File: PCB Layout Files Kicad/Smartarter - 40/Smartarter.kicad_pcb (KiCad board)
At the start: 2 copper layers, 135.5 x 154.5 mm, 44 parts, among them J1 Screw_Terminal_01x03, J2 Screw_Terminal_01x03, K1 onRelay, K2 offRelay, Q1 BC547, Q2 BC547, Q3 BC547, SW1 SW_Push, U1 74164, U2 KCSA02-107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

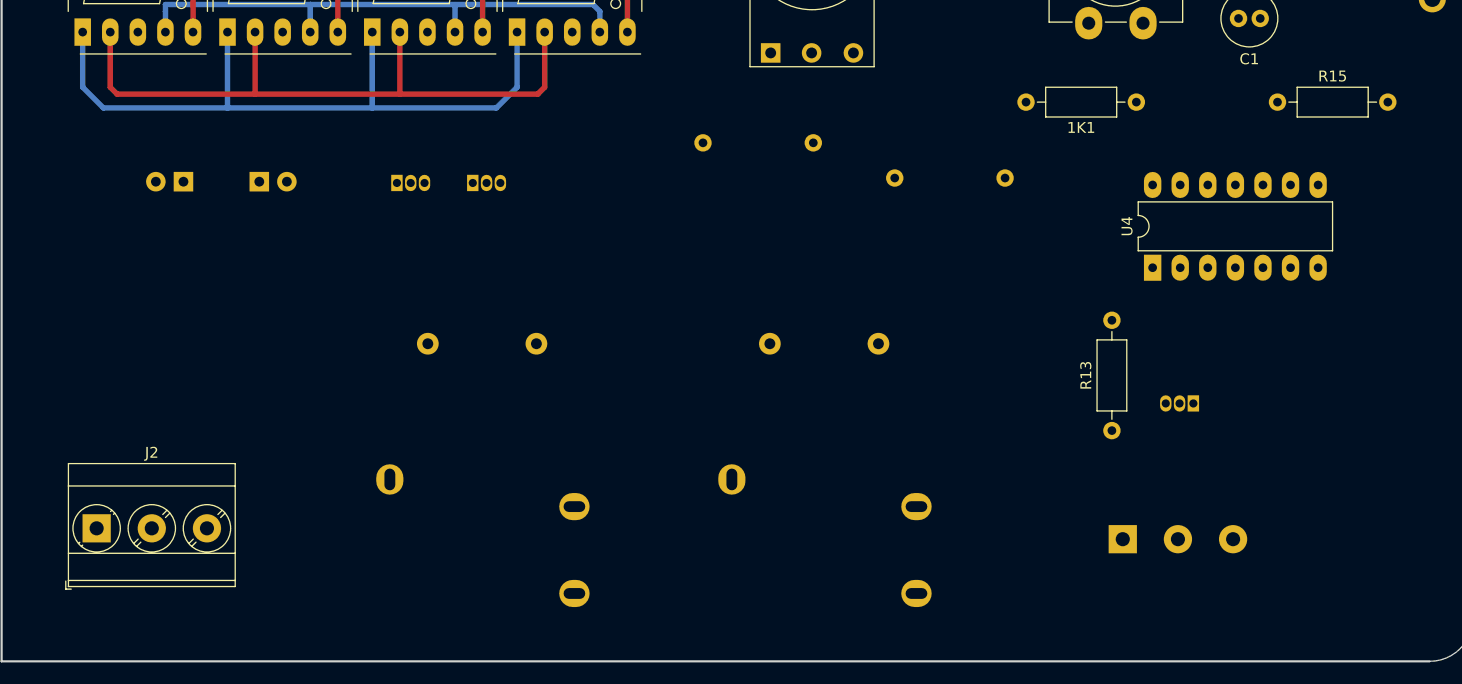
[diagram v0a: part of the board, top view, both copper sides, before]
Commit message: inductor and full wave rectifier implemented in both schematic and layout
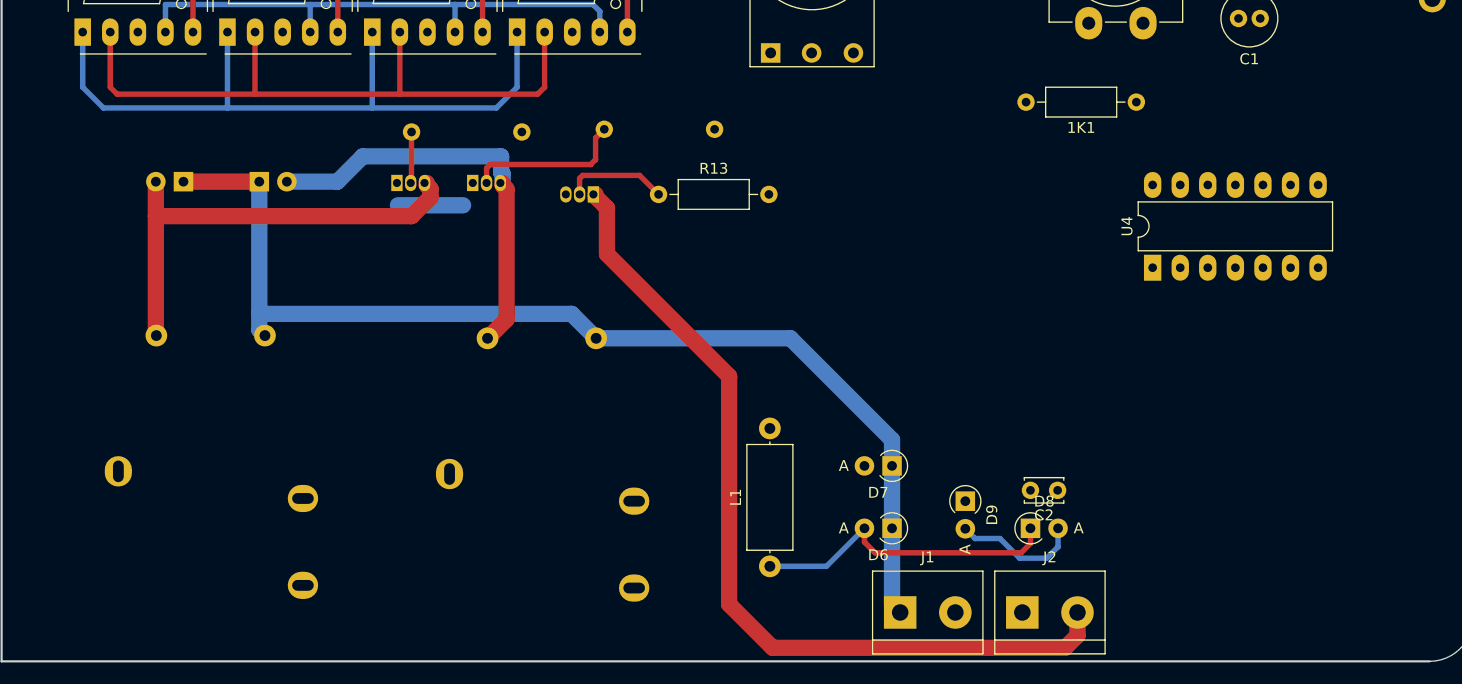
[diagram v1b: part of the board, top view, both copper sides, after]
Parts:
- removed R15: R, Resistor_THT:R_Axial_DIN0207_L6.3mm_D2.5mm_P10.16mm_Horizontal
- added C2: C_Small, Capacitor_THT:C_Disc_D3.4mm_W2.1mm_P2.50mm, F.Cu at (146.2, 164.8)
- added D6: DIODE, Diode_THT:D_A-405_P2.54mm_Vertical_AnodeUp, F.Cu at (131.0, 168.2)
- added D7: DIODE, Diode_THT:D_A-405_P2.54mm_Vertical_AnodeUp, F.Cu at (131.0, 162.5)
- added D8: DIODE, Diode_THT:D_A-405_P2.54mm_Vertical_AnodeUp, F.Cu at (143.8, 168.2)
- added D9: DIODE, Diode_THT:D_A-405_P2.54mm_Vertical_AnodeUp, F.Cu at (137.8, 165.8)
- added L1: INDUCTOR, Inductor_THT:L_Axial_L9.5mm_D4.0mm_P12.70mm_Horizontal_Fastron_SMCC, F.Cu at (119.8, 171.8)
- J1: value Screw_Terminal_01x03 -> Screw_Terminal_01x02; footprint Connector_Phoenix:TerminalBlock_Phoenix_MKDS-3-3-5.08_1x03_P5.08mm_Horizontal -> TerminalBlock:TerminalBlock_bornier-2_P5.08mm; moved to F.Cu
- J2: value Screw_Terminal_01x03 -> Screw_Terminal_01x02; footprint Connector_Phoenix:TerminalBlock_Phoenix_MKDS-3-3-5.08_1x03_P5.08mm_Horizontal -> TerminalBlock:TerminalBlock_bornier-2_P5.08mm
- moved J2 85.6 mm to (143.0, 176.0)
- moved Q3 58.5 mm to (103.5, 137.5)
- moved R13 47.1 mm to (109.5, 137.5), turned to 0 degrees
- moved 10K2 37.0 mm to (86.8, 131.8), turned to 0 degrees
- moved 10K3 27.1 mm to (104.5, 131.5)
- moved K1 26.0 mm to (112.8, 143.8)
- moved K2 25.0 mm to (82.2, 143.5)
- moved J1 21.6 mm to (131.8, 176.0)
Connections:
- A1 pad 14: (no net) -> Net-(A1-Pad14)
- J1 pad 1: Net-(J1-Pad1) -> GND
- J1 pad 2: GND -> Net-(J1-Pad2)
- J2 pad 2: GND -> +12V
- Q3 pad 3: Net-(J1-Pad3) -> Net-(J1-Pad2)
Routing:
- net GND: track 47.4 -> 148.1 mm
- net +12V: track 0.00 -> 79.2 mm
- net Net-(D5-Pad2): track 0.00 -> 41.7 mm
- net Net-(D4-Pad2): track 0.00 -> 38.4 mm
- net Net-(D6-Pad2): track 0.00 -> 28.9 mm
- net Net-(10K3-Pad1): track 0.00 -> 14.9 mm
- net Net-(A1-Pad14): track 0.00 -> 11.8 mm
- net Net-(Q3-Pad2): track 0.00 -> 9.59 mm
- net (no net): track 0.00 -> 6.00 mm
- net Net-(10K2-Pad1): track 0.00 -> 4.73 mm

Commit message: chaar bilang chhota kar diya
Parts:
- added REF**: SolderWirePad_1x01_Drill2mm, Connector_Wire:SolderWirePad_1x01_Drill2mm, F.Cu at (85.9, 128.7)
- added REF**: SolderWirePad_1x01_Drill2mm, Connector_Wire:SolderWirePad_1x01_Drill2mm, F.Cu at (110.7, 128.7)
- moved C2 153.1 mm to (72.2, 30.8), turned to 270 degrees
- moved J2 149.2 mm to (113.2, 29.8), turned to 180 degrees
- moved J1 149.2 mm to (102.2, 29.8), turned to 180 degrees
- moved D9 148.6 mm to (80.2, 28.8), turned to 180 degrees
- moved D8 148.1 mm to (80.2, 34.5), turned to 180 degrees
- moved D6 140.5 mm to (88.0, 34.5)
- moved D7 140.5 mm to (88.0, 28.8)
- moved R13 99.3 mm to (99.7, 38.7)
- moved Q3 99.0 mm to (95.4, 38.8)
- moved U4 98.6 mm to (177.5, 48.2), turned to 180 degrees
- moved C1 68.2 mm to (177.6, 54.3), turned to 0 degrees
- moved R11 62.1 mm to (114.8, 100.0), turned to 90 degrees
- moved R8 57.9 mm to (72.6, 104.0), turned to 225 degrees
- moved K1 51.6 mm to (150.7, 108.8), turned to 0 degrees
- moved K2 49.8 mm to (118.0, 108.8), turned to 0 degrees
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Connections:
- J1 pad 1: GND -> +12V
- J2 pad 2: +12V -> GND
- U3 pad 2: Net-(R12-Pad2) -> (no net)
- U3 pad 3: +5V -> (no net)
- U3 pad 5: (no net) -> Net-(R12-Pad2)
- U3 pad 6: (no net) -> +5V
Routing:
- net GND: track 148.1 -> 363.8 mm
- net (no net): track 6.00 -> 144.0 mm
- net +5V: track 7.62 -> 87.3 mm
- net +12V: track 79.2 -> 0.00 mm
- net Net-(R8-Pad2): track 43.1 -> 0.00 mm
- net Net-(D4-Pad2): track 38.4 -> 73.9 mm
- net Net-(R9-Pad2): track 34.3 -> 0.00 mm
- net Net-(R10-Pad2): track 33.9 -> 0.00 mm
- net Net-(R11-Pad2): track 27.8 -> 0.00 mm
- net Net-(10K1-Pad2): track 0.00 -> 27.0 mm
- net Net-(D6-Pad2): track 28.9 -> 5.21 mm
- net Net-(R12-Pad2): track 0.00 -> 15.3 mm
- net Net-(R6-Pad2): track 13.2 -> 0.00 mm
- net Net-(R4-Pad2): track 12.1 -> 0.00 mm
- net Net-(R7-Pad2): track 11.0 -> 0.00 mm
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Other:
- board size 135.5 x 154.5 mm -> 135.5 x 111.5 mm
